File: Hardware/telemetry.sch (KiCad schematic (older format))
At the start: 1 part, among them U5 RA-02_LORA

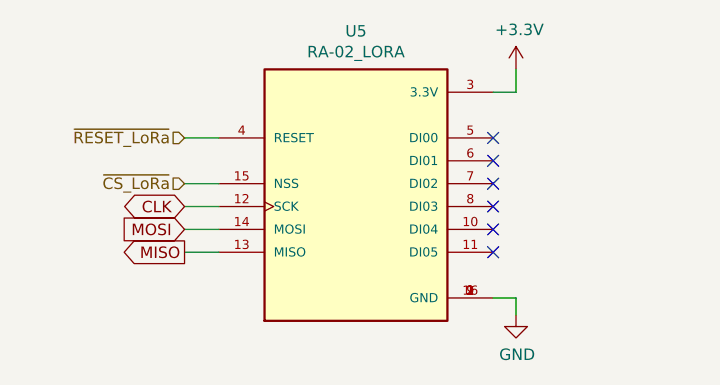
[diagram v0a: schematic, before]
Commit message: Update schematic, component placement
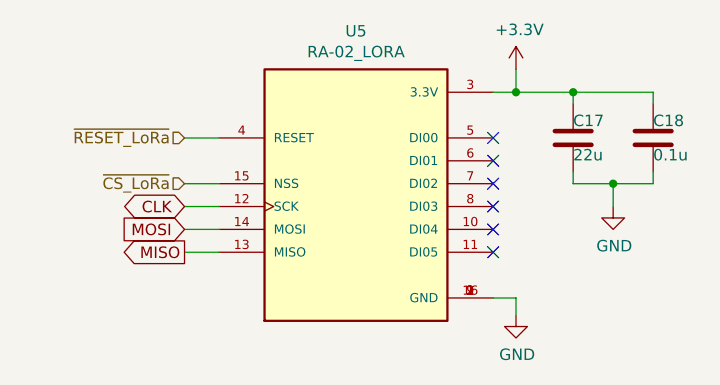
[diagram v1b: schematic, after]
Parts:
- added C17: 22u, Capacitor_SMD:C_0603_1608Metric, symbol Device:C
- added C18: 0.1u, Capacitor_SMD:C_0603_1608Metric, symbol Device:C
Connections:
- net +3V3: now also C17.1, C18.1
- net GND: now also C17.2, C18.2
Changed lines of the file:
@@
 Text GLabel 5000 4350 0    50   BiDi ~ 0
 CLK
+$Comp
+L Device:C C17
+U 1 1 611962D4
+P 6700 4050
+F 0 "C17" H 6700 4125 50  0000 L CNN
+F 1 "22u" H 6700 3975 50  0000 L CNN
+F 2 "Capacitor_SMD:C_0603_1608Metric" H 6738 3900 50  0001 C CNN
+F 3 "~" H 6700 4050 50  0001 C CNN
+	1    6700 4050
+	1    0    0    -1
+$EndComp
+Wire Wire Line
+	6450 3850 6700 3850
+Connection ~ 6450 3850
+Connection ~ 6700 3850
+$Comp
+L Device:C C18
+U 1 1 61196CD3
+P 7050 4050
+F 0 "C18" H 7050 4125 50  0000 L CNN
+F 1 "0.1u" H 7050 3975 50  0000 L CNN
+F 2 "Capacitor_SMD:C_0603_1608Metric" H 7088 3900 50  0001 C CNN
+F 3 "~" H 7050 4050 50  0001 C CNN
+	1    7050 4050
+	1    0    0    -1
+$EndComp
+Wire Wire Line
+	6700 3850 6700 3900
+Wire Wire Line
+	7050 3850 7050 3900
+Wire Wire Line
+	6700 3850 7050 3850
+Wire Wire Line
+	6700 4200 6700 4250
+Wire Wire Line
+	6700 4250 6875 4250
+Wire Wire Line
+	7050 4250 7050 4200
+$Comp
+L power:GND #PWR032
+U 1 1 61197B2A
+P 6875 4350
+F 0 "#PWR032" H 6875 4100 50  0001 C CNN
+F 1 "GND" H 6880 4177 50  0000 C CNN
+F 2 "" H 6875 4350 50  0001 C CNN
+F 3 "" H 6875 4350 50  0001 C CNN
+	1    6875 4350
+	1    0    0    -1
+$EndComp
+Wire Wire Line
+	6875 4350 6875 4250
+Connection ~ 6875 4250
+Wire Wire Line
+	6875 4250 7050 4250
 $EndSCHEMATC

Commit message: Change regulator diode footprint, update routing
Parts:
- U5: Manufacturer_Part_Number (none) -> Ra-02
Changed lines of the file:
@@
 F 6 "Ai-Thinker" H 5750 4350 50  0001 L BNN "MANUFACTURER"
 F 7 "3.3mm" H 5750 4350 50  0001 L BNN "MAXIMUM_PACKAGE_HEIGHT"
+F 8 "Ra-02" H 5750 4350 50  0001 C CNN "Manufacturer_Part_Number"
 	1    5750 4350
 	1    0    0    -1
